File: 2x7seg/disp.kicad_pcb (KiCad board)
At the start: 2 copper layers, 35.8 x 30.5 mm, 11 parts, among them P1 CONN_01X08, P2 CONN_01X08, U1 TLC59282, U2 LDD-A814RI

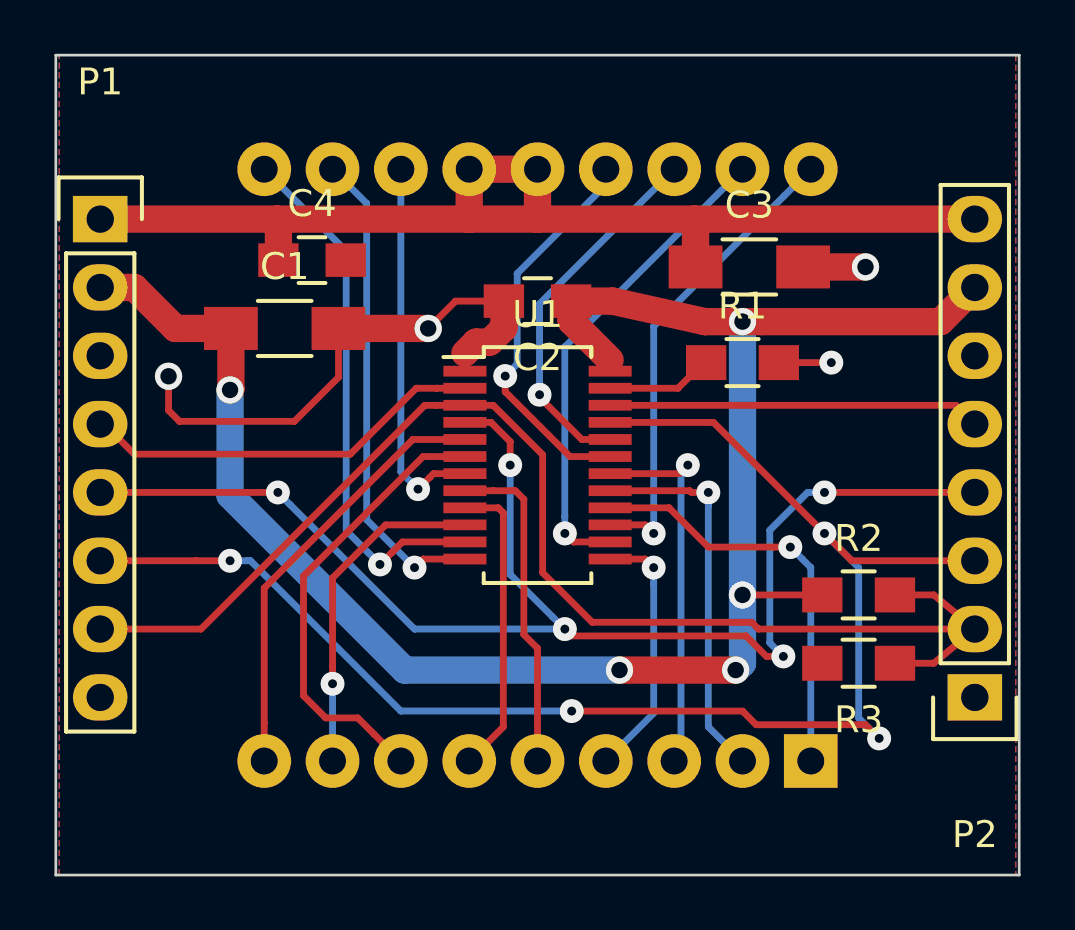
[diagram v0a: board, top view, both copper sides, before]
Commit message: Adjust the pin drill size for the 7-seg display.
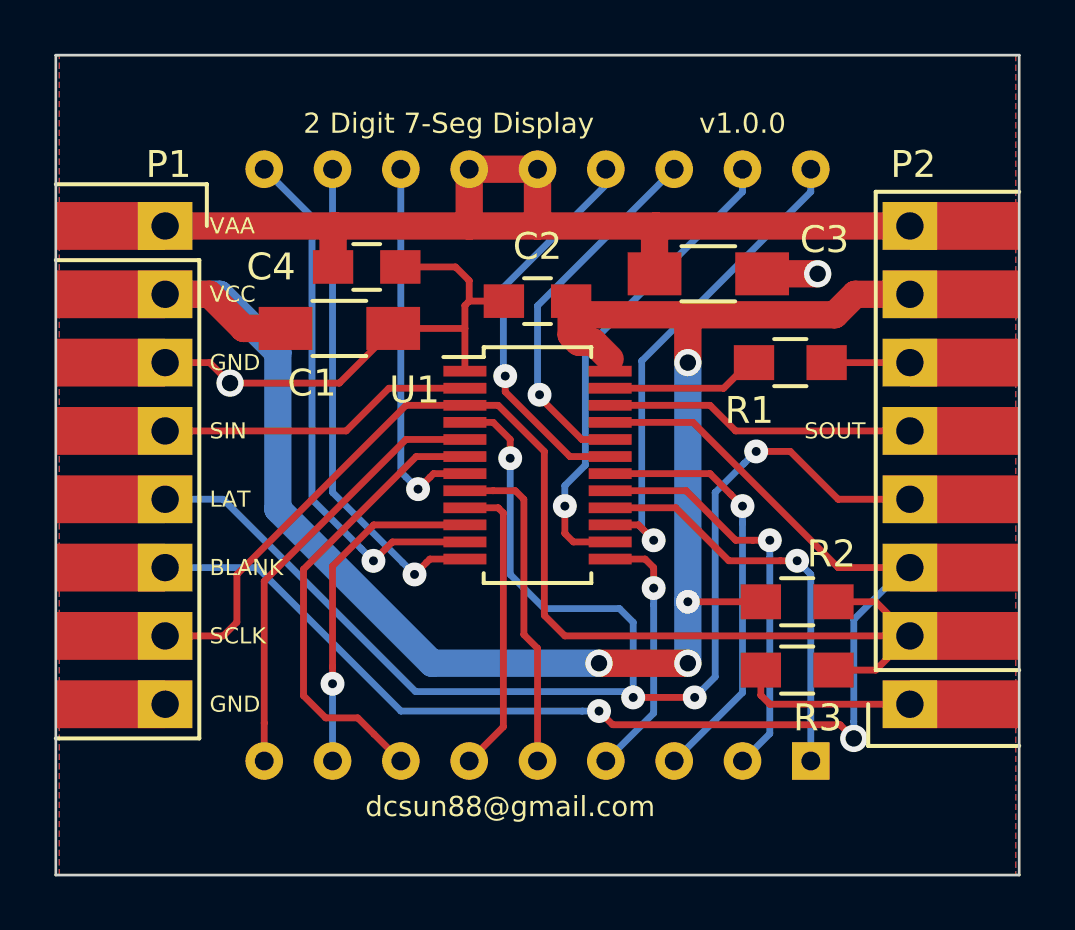
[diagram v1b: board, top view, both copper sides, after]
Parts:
- P1, P2: footprint Pin_Headers:Pin_Header_Straight_1x08 -> local:Pin_Header_1x08_edge
- moved P2 2.43 mm to (158.4, 103.6)
- moved P1 2.43 mm to (130.7, 85.9)
- moved R2 2.30 mm to (154.2, 99.8)
- moved R3 2.30 mm to (154.2, 102.4)
- moved C4 2.05 mm to (138.2, 87.4)
- moved C1 2.03 mm to (137.2, 89.7)
- moved R1 1.78 mm to (153.9, 90.9)
- moved C3 1.55 mm to (150.9, 87.6)
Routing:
- net GND: track 24.7 -> 33.6 mm, vias 4 -> 2
- net /BLANK: track 55.8 -> 48.9 mm, vias 4 -> 2
- net VAA: track 42.1 -> 37.8 mm
- net /LAT: track 50.8 -> 54.3 mm, vias 5 -> 4
- net /SIN: track 15.0 -> 11.8 mm
- net /SCLK: track 48.8 -> 46.2 mm
- net VCC: track 68.2 -> 65.8 mm, vias 5 -> 4
- net /SOUT: track 13.8 -> 11.5 mm
- net /IREF: track 3.76 -> 5.57 mm
- net /D1c: track 14.2 -> 15.9 mm
- net /D1d: track 14.2 -> 15.3 mm
- net /D1f: track 17.7 -> 18.4 mm
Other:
- board text added: "2 Digit 7-Seg Display"
- board text added: "BLANK"
- board text added: "GND"
- board text added: "LAT"
- board text added: "SCLK"
- board text added: "SIN"
- board text added: "SOUT"
- board text added: "VAA"
- board text added: "VCC"
- board text added: "dcsun88@gmail.com"
- board text added: "v1.0.0"

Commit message: Optimize some of the ground fill.
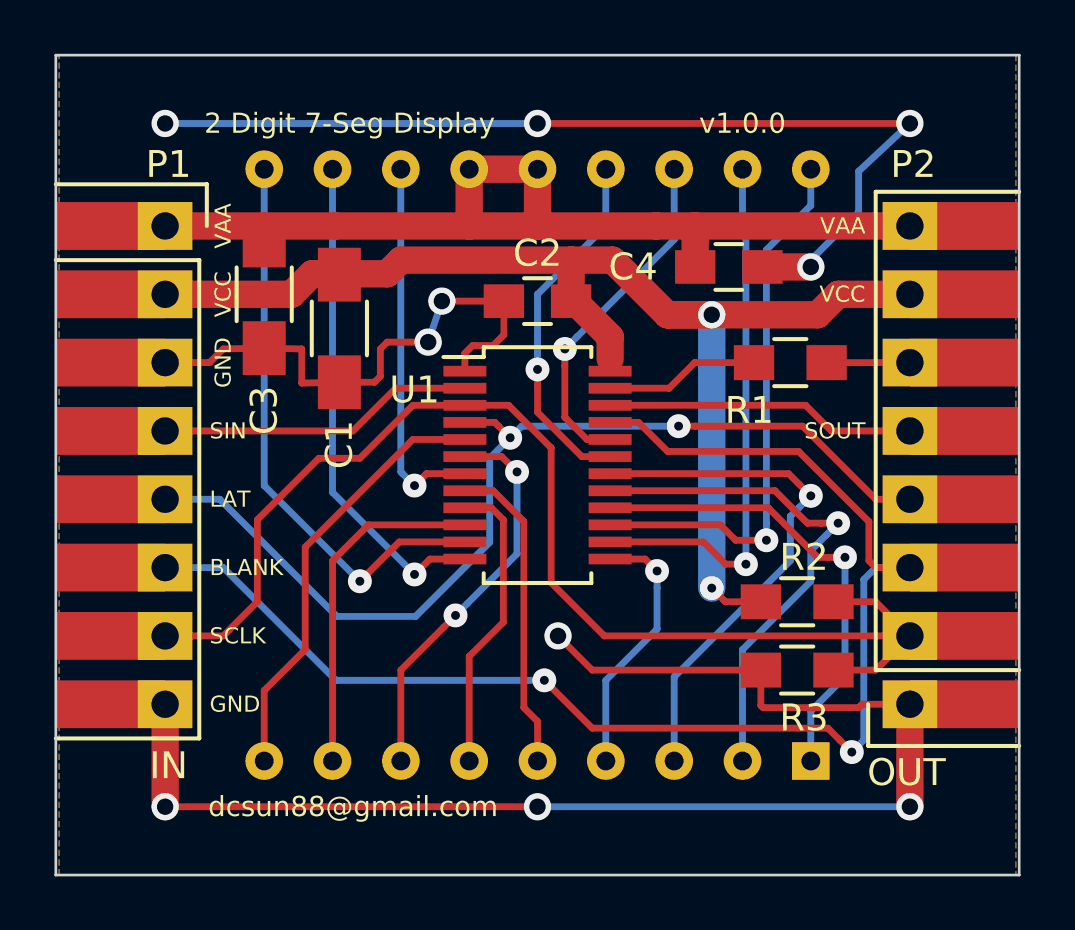
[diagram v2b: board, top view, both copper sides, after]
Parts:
- moved C3 16.5 mm to (134.4, 88.4), turned to 270 degrees
- moved C4 13.5 mm to (151.6, 87.4)
- turned C1 to 270 degrees
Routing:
- net GND: track 33.6 -> 115.9 mm, vias 2 -> 10
- net /LAT: track 54.3 -> 37.3 mm, vias 4 -> 2
- net VCC: track 65.8 -> 52.1 mm, vias 4 -> 2
- net /BLANK: track 48.9 -> 53.4 mm
- net /SCLK: track 46.2 -> 50.3 mm
- net /D1d: track 15.3 -> 19.3 mm
- net /D1c: track 15.9 -> 19.8 mm
- net /D2g: track 17.1 -> 14.7 mm, vias 0 -> 2
- net /D1e: track 15.4 -> 17.6 mm
- net /D1f: track 18.4 -> 20.5 mm
- net /D1g: track 18.1 -> 20.1 mm
- net /SOUT: track 11.5 -> 13.6 mm
- net /SIN: track 11.8 -> 13.8 mm
- net /D2b: track 19.9 -> 21.3 mm
- net VAA: track 37.8 -> 36.5 mm
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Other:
- board text added: "IN"
- board text added: "OUT"

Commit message: Fix minimum annular ring. Use 10mil minimum clearance.
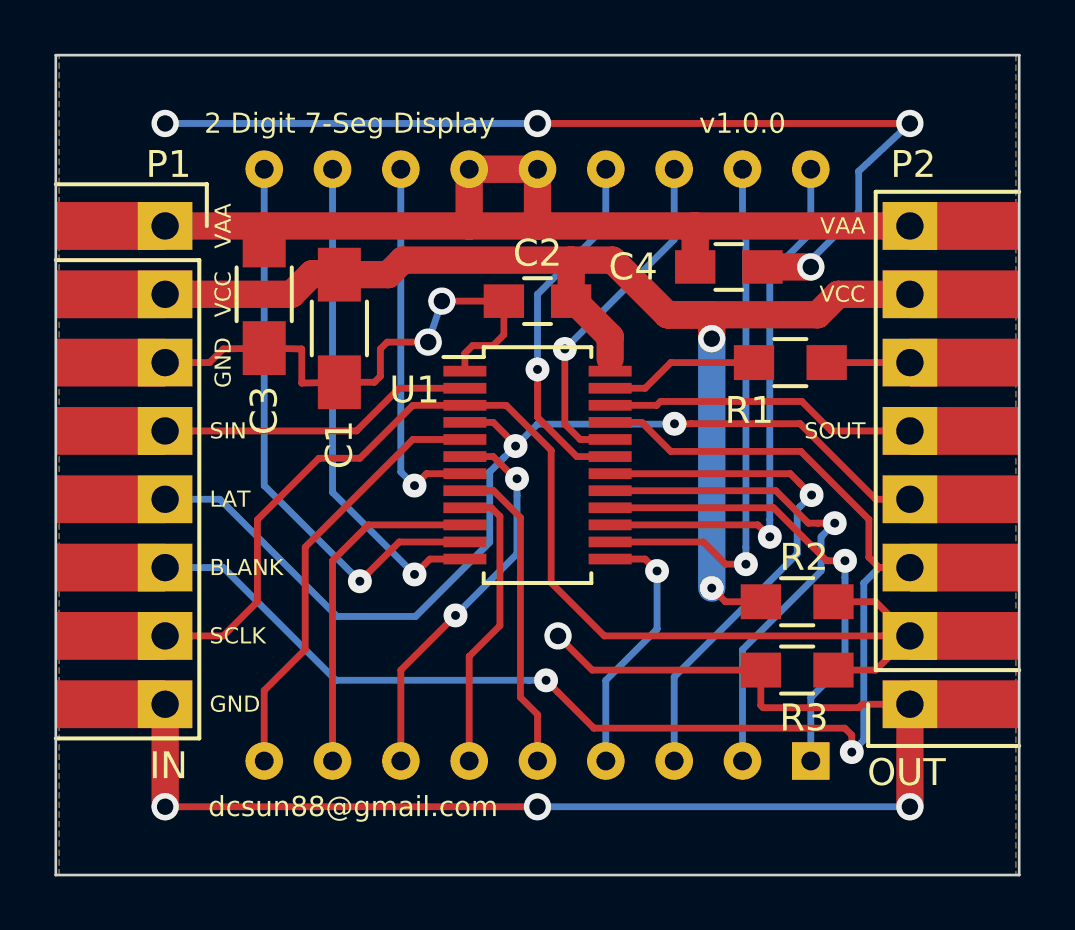
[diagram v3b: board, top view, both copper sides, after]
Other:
- net class minimum: via_dia 0.508 -> 0.6858
- rule via_min_size: 0.508 -> 0.6858
